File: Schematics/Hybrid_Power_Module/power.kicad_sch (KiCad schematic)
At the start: 97 parts, among them J1 ScrewSwitch, J2 Battery, J3 ScrewSwitch, J4 GSE, J7 Stack Male Edge Connector, Q1 AO4447A, Q2 SI2305CDS, Q3 DMN6040SSD-13, U1 TPS61175PWPR, U10 LM66100DCKR, U11 LM66100DCKR, U12 AMS1117-3.3, U2 LM74700QDBVRQ1, U3 LM74700QDBVRQ1, U4 ACS37041KLHBLT-010B3, U5 ACS37041KLHBLT-010B5, U6 INA187A, U7 LMR51430XDDCR, U8 LMR51430XDDCR, U9 LM66100DCKR

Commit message: fix: Updates after testing, for next revision
 - add current limiting to GSE RPP zener shunt
 - switched 5v current sensor
 - flipped CAN and UART polarity
 - add 3.3v reference to CAN transceiver
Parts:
- added R31: 9.1k, Resistor_SMD:R_0603_1608Metric, symbol Device:R
- added R32: 15k, Resistor_SMD:R_0603_1608Metric, symbol Device:R
- U5: value ACS37041KLHBLT-010B5 -> ACS37041KLHBLT-010B3; Digikey 620-ACS37041KLHBLT-010B5CT-ND -> 620-ACS37041KLHBLT-010B3CT-ND
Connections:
- net 24V_GSE: now also R31.1
- net CAN_N: now also J7.B13 (CAN_L); no longer J7.B14 (CAN_H)
- net CAN_P: now also J7.B14 (CAN_H); no longer J7.B13 (CAN_L)
- net GND: now also R32.2; no longer D3.2 (A), Q2.1 (G)
- new net: D3.2 (A), Q2.1 (G), R31.2, R32.1
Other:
- note added: "- TVS: clamps pos and neg rails (breakdown 31.1V) - P-MOSFET: RPP switch, VGS_max = +-20V - 12V ZENER: reverse bias Vgs = 0 - 12 = -12V, forward bias Vgs = 24 - 23.3 = 0.7v - can the zener handle the current? ya it can"t!!! next revision I guess"
- note added: "for next revision Fixed 5v current sensor"
- note added: "for next revision Fixed CAN P/N polarity"
- note added: "for next revision Zener Pmax = 400mW At full 24V on the cathode Iz = 400mW/12V = 33.3mA R = 12^2/400mW = 360ohms Vgs optimal for RDS(on) = -8V to -10V R1/(R1+R2) = 9.1/(9.1+15) = 0.378 R1 = 9.1kohms R2 = 15kohms"
- note removed: "- TVS: clamps pos and neg rails (breakdown 31.1V) - P-MOSFET: RPP switch, VGS_max = +-20V - 12V ZENER: reverse bias Vgs = 0 - 12 = -12V, forward bias Vgs = 24 - 23.3 = 0.7v - can the zener handle the current?"

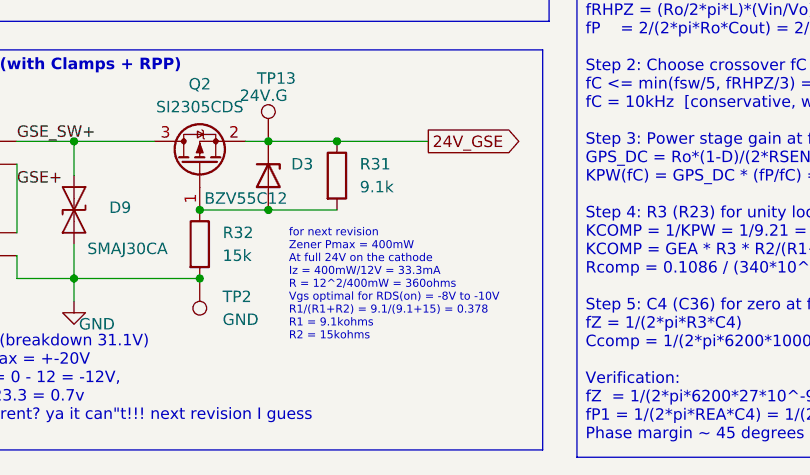
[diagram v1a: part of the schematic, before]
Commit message: Update RPP circuit to reflect R31 and R32 values used for fix
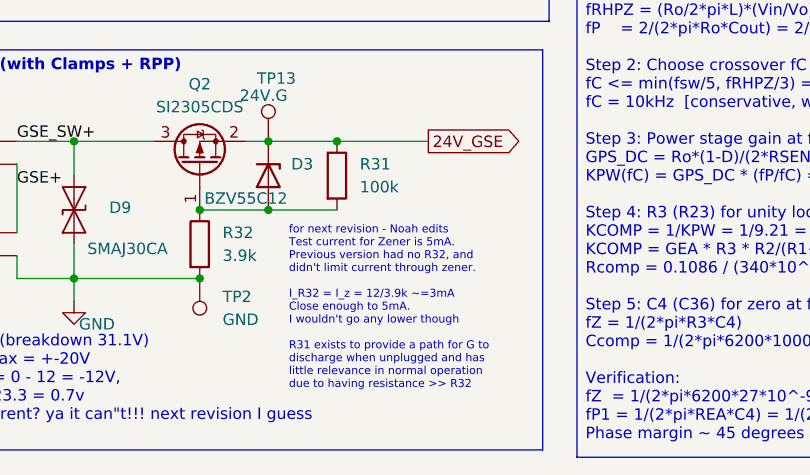
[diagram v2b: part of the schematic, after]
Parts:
- R31: value 9.1k -> 100k
- R32: value 15k -> 3.9k
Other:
- note added: "for next revision - Noah edits Test current for Zener is 5mA. Previous version had no R32, and didn't limit current through zener. I_R32 = I_z = 12/3.9k ~=3mA Close enough to 5mA. I wouldn't go any lower though R31 exists to provide a path for G to discharge when unplugged and has little relevance in normal operation due to having resistance >> R32"
- note removed: "for next revision Zener Pmax = 400mW At full 24V on the cathode Iz = 400mW/12V = 33.3mA R = 12^2/400mW = 360ohms Vgs optimal for RDS(on) = -8V to -10V R1/(R1+R2) = 9.1/(9.1+15) = 0.378 R1 = 9.1kohms R2 = 15kohms"
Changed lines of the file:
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@@
 		)
 	)
-	(text "for next revision\nZener Pmax = 400mW\nAt full 24V on the cathode\nIz = 400mW/12V = 33.3mA\nR = 12^2/400mW = 360ohms\nVgs optimal for RDS(on) = -8V to -10V\nR1/(R1+R2) = 9.1/(9.1+15) = 0.378\nR1 = 9.1kohms\nR2 = 15kohms"
+	(text "for next revision - Noah edits\nTest current for Zener is 5mA. \nPrevious version had no R32, and \ndidn't limit current through zener.\n\nI_R32 = I_z = 12/3.9k ~=3mA\nClose enough to 5mA. \nI wouldn't go any lower though\n\nR31 exists to provide a path for G to \ndischarge when unplugged and has \nlittle relevance in normal operation \ndue to having resistance >> R32"
 		(exclude_from_sim no)
-		(at 74.676 263.652 0)
+		(at 74.676 266.192 0)
 		(effects
 			(font
@@
 			)
 		)
-		(property "Value" "15k"
+		(property "Value" "3.9k"
 			(at 67.31 260.3499 0)
 			(show_name no)
@@
 			)
 		)
-		(property "Value" "9.1k"
+		(property "Value" "100k"
 			(at 82.55 252.7299 0)
 			(show_name no)
